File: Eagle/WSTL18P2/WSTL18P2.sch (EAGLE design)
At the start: 23 parts, among them CON1 1X6CONN-1.27-ROUND, CON2 1X6CONN-1.27-ROUND, CON3 1X6CONN-1.27-ROUND, CON4 1X6CONN-1.27-ROUND, T1 ABS07AIG

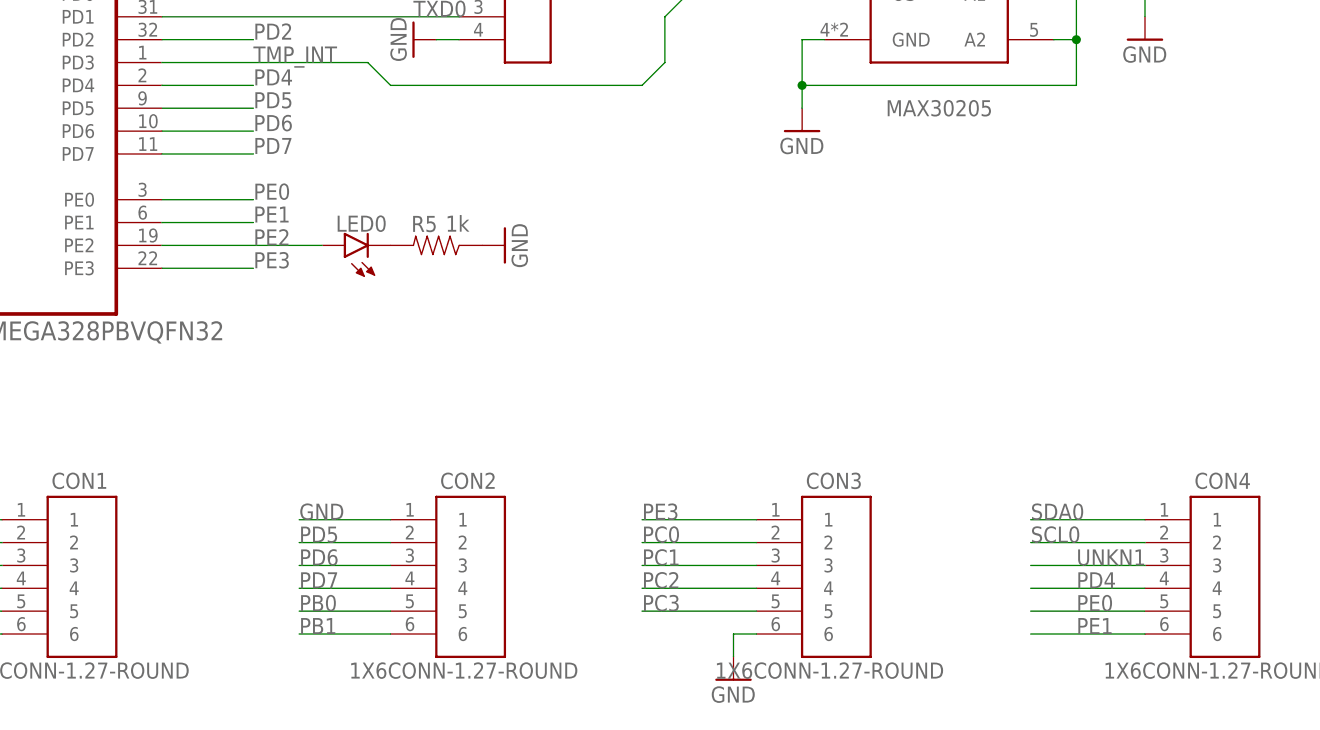
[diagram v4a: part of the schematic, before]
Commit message: Chaned LED pin, added VCC and GND next to TWI(I2C) headers, changed some traces to 8mil
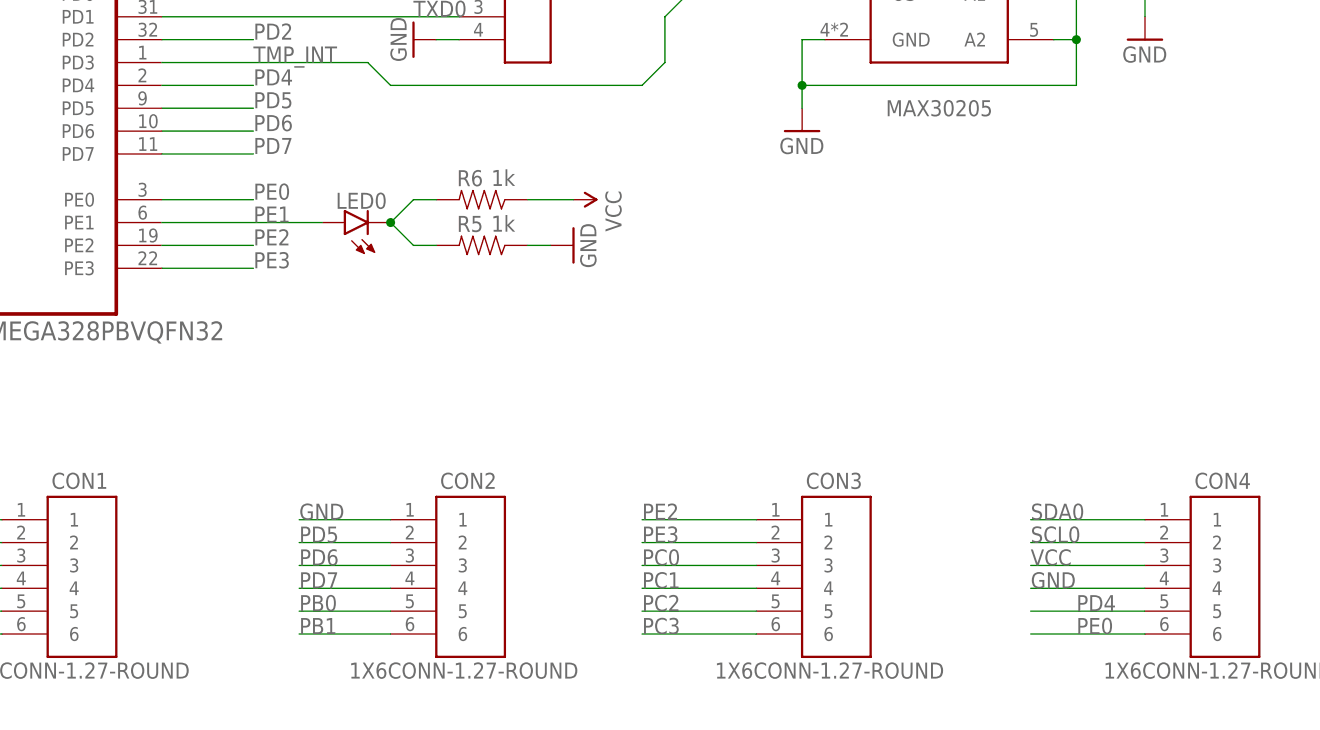
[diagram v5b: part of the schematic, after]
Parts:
- added R6: 1k, Passives:RES_0402_CERAMIC
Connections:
- removed net UNKN1: CON4.3
- net GND: now also CON4.4; no longer CON3.6
- net N$4: now also R6.1
- net PC0: now also CON3.3; no longer CON3.2
- net PC1: now also CON3.4; no longer CON3.3
- net PC2: now also CON3.5; no longer CON3.4
- net PC3: now also CON3.6; no longer CON3.5
- net PD4: now also CON4.5; no longer CON4.4
- net PE0: now also CON4.6; no longer CON4.5
- net PE1: now also LED0.A; no longer CON4.6
- net PE2: now also CON3.1; no longer LED0.A
- net PE3: now also CON3.2; no longer CON3.1
- net VCC: now also CON4.3, R6.2
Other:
- moved on the sheet: LED0, R5
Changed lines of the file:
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@@
 <part name="CON2" library="AVR_ISP_127" deviceset="1X6CONN-1.27-ROUND" device=""/>
 <part name="CON3" library="AVR_ISP_127" deviceset="1X6CONN-1.27-ROUND" device=""/>
-<part name="GND9" library="SparkFun-Aesthetics" deviceset="GND" device=""/>
 <part name="CON4" library="AVR_ISP_127" deviceset="1X6CONN-1.27-ROUND" device=""/>
 <part name="VCC" library="SparkFun-Aesthetics" deviceset="5V" device="" value="VCC"/>
@@
 <part name="GND10" library="SparkFun-Aesthetics" deviceset="GND" device=""/>
 <part name="GND12" library="SparkFun-Aesthetics" deviceset="GND" device=""/>
+<part name="VCC1" library="SparkFun-Aesthetics" deviceset="5V" device="" value="VCC"/>
+<part name="R6" library="Passives" deviceset="RES_0402_CERAMIC" device="" value="1k"/>
 </parts>
 <sheets>
@@
 </instance>
 <instance part="R1" gate="G$1" x="50.8" y="-12.7" rot="R90"/>
-<instance part="LED0" gate="G$1" x="106.68" y="22.86" smashed="yes" rot="R90">
-<attribute name="NAME" x="105.664" y="24.384" size="1.778" layer="95"/>
-</instance>
-<instance part="GND8" gate="1" x="124.46" y="22.86" rot="R90"/>
-<instance part="R5" gate="G$1" x="116.84" y="22.86" smashed="yes" rot="R180">
-<attribute name="NAME" x="114.046" y="24.3586" size="1.778" layer="95"/>
-<attribute name="VALUE" x="117.856" y="24.384" size="1.778" layer="96"/>
+<instance part="LED0" gate="G$1" x="106.68" y="25.4" smashed="yes" rot="R90">
+<attribute name="NAME" x="105.664" y="26.924" size="1.778" layer="95"/>
+</instance>
+<instance part="GND8" gate="1" x="132.08" y="22.86" rot="R90"/>
+<instance part="R5" gate="G$1" x="121.92" y="22.86" smashed="yes" rot="R180">
+<attribute name="NAME" x="119.126" y="24.3586" size="1.778" layer="95"/>
+<attribute name="VALUE" x="122.936" y="24.384" size="1.778" layer="96"/>
 </instance>
 <instance part="R4" gate="G$1" x="154.94" y="68.58" smashed="yes" rot="R90">
@@
 <instance part="CON2" gate="G$1" x="121.92" y="-10.16"/>
 <instance part="CON3" gate="G$1" x="162.56" y="-10.16"/>
-<instance part="GND9" gate="1" x="149.86" y="-25.4"/>
 <instance part="CON4" gate="G$1" x="205.74" y="-10.16"/>
 <instance part="VCC" gate="G$1" x="-76.2" y="76.2"/>
@@
 <instance part="GND10" gate="1" x="43.18" y="12.7"/>
 <instance part="GND12" gate="1" x="17.78" y="12.7"/>
+<instance part="VCC1" gate="G$1" x="132.08" y="27.94" rot="R270"/>
+<instance part="R6" gate="G$1" x="121.92" y="27.94" smashed="yes" rot="R180">
+<attribute name="NAME" x="119.126" y="29.4386" size="1.778" layer="95"/>
+<attribute name="VALUE" x="122.936" y="29.464" size="1.778" layer="96"/>
+</instance>
 </instances>
 <busses>
@@
 <wire x1="48.26" y1="76.2" x2="48.26" y2="71.12" width="0.1524" layer="91"/>
 <junction x="48.26" y="71.12"/>
+</segment>
+<segment>
+<pinref part="R6" gate="G$1" pin="2"/>
+<pinref part="VCC1" gate="G$1" pin="5V"/>
+<wire x1="127" y1="27.94" x2="132.08" y2="27.94" width="0.1524" layer="91"/>
+</segment>
+<segment>
+<label x="182.88" y="-12.7" size="1.778" layer="95"/>
+<wire x1="182.88" y1="-12.7" x2="195.58" y2="-12.7" width="0.1524" layer="91"/>
+<pinref part="CON4" gate="G$1" pin="3"/>
 </segment>
 </net>
@@
 <pinref part="GND8" gate="1" pin="GND"/>
 <pinref part="R5" gate="G$1" pin="2"/>
+<wire x1="127" y1="22.86" x2="129.54" y2="22.86" width="0.1524" layer="91"/>
 </segment>
 <segment>
@@
 </segment>
 <segment>
-<pinref part="GND9" gate="1" pin="GND"/>
-<wire x1="149.86" y1="-20.32" x2="149.86" y2="-22.86" width="0.1524" layer="91"/>
-<pinref part="CON3" gate="G$1" pin="6"/>
-<wire x1="149.86" y1="-20.32" x2="152.4" y2="-20.32" width="0.1524" layer="91"/>
-</segment>
-<segment>
 <pinref part="GND11" gate="1" pin="GND"/>
 <pinref part="UART" gate="G$1" pin="4"/>
@@
 <pinref part="C7" gate="G$1" pin="2"/>
 <wire x1="43.18" y1="15.24" x2="43.18" y2="17.78" width="0.1524" layer="91"/>
+</segment>
+<segment>
+<pinref part="CON4" gate="G$1" pin="4"/>
+<wire x1="195.58" y1="-15.24" x2="182.88" y2="-15.24" width="0.1524" layer="91"/>
+<label x="182.88" y="-15.24" size="1.778" layer="95"/>
 </segment>
 </net>
@@
 <pinref part="LED0" gate="G$1" pin="C"/>
 <pinref part="R5" gate="G$1" pin="1"/>
+<wire x1="111.76" y1="25.4" x2="114.3" y2="22.86" width="0.1524" layer="91"/>
+<wire x1="114.3" y1="22.86" x2="116.84" y2="22.86" width="0.1524" layer="91"/>
+<wire x1="111.76" y1="25.4" x2="114.3" y2="27.94" width="0.1524" layer="91"/>
+<junction x="111.76" y="25.4"/>
+<pinref part="R6" gate="G$1" pin="1"/>
+<wire x1="114.3" y1="27.94" x2="116.84" y2="27.94" width="0.1524" layer="91"/>
 </segment>
 </net>
@@
 </segment>
 <segment>
-<label x="187.96" y="-15.24" size="1.778" layer="95"/>
-<pinref part="CON4" gate="G$1" pin="4"/>
-<wire x1="182.88" y1="-15.24" x2="195.58" y2="-15.24" width="0.1524" layer="91"/>
+<label x="187.96" y="-17.78" size="1.778" layer="95"/>
+<wire x1="182.88" y1="-17.78" x2="195.58" y2="-17.78" width="0.1524" layer="91"/>
+<pinref part="CON4" gate="G$1" pin="5"/>
 </segment>
 </net>
@@
 </segment>
 <segment>
-<label x="187.96" y="-17.78" size="1.778" layer="95"/>
-<wire x1="182.88" y1="-17.78" x2="195.58" y2="-17.78" width="0.1524" layer="91"/>
-<pinref part="CON4" gate="G$1" pin="5"/>
+<label x="187.96" y="-20.32" size="1.778" layer="95"/>
+<wire x1="182.88" y1="-20.32" x2="195.58" y2="-20.32" width="0.1524" layer="91"/>
+<pinref part="CON4" gate="G$1" pin="6"/>
 </segment>
 </net>
@@
 <segment>
 <pinref part="MCU" gate="A" pin="PE1"/>
-<wire x1="86.36" y1="25.4" x2="96.52" y2="25.4" width="0.1524" layer="91"/>
+<wire x1="86.36" y1="25.4" x2="104.14" y2="25.4" width="0.1524" layer="91"/>
 <label x="96.52" y="25.4" size="1.778" layer="95"/>
-</segment>
-<segment>
-<wire x1="195.58" y1="-20.32" x2="182.88" y2="-20.32" width="0.1524" layer="91"/>
-<label x="187.96" y="-20.32" size="1.778" layer="95"/>
-<pinref part="CON4" gate="G$1" pin="6"/>
+<pinref part="LED0" gate="G$1" pin="A"/>
 </segment>
 </net>
@@
 </segment>
 <segment>
-<wire x1="152.4" y1="-7.62" x2="139.7" y2="-7.62" width="0.1524" layer="91"/>
-<label x="139.7" y="-7.62" size="1.778" layer="95"/>
-<pinref part="CON3" gate="G$1" pin="1"/>
+<label x="139.7" y="-10.16" size="1.778" layer="95"/>
+<wire x1="152.4" y1="-10.16" x2="139.7" y2="-10.16" width="0.1524" layer="91"/>
+<pinref part="CON3" gate="G$1" pin="2"/>
 </segment>
 </net>
@@
 </segment>
 <segment>
-<pinref part="CON3" gate="G$1" pin="3"/>
-<wire x1="152.4" y1="-12.7" x2="139.7" y2="-12.7" width="0.1524" layer="91"/>
-<label x="139.7" y="-12.7" size="1.778" layer="95"/>
+<label x="139.7" y="-15.24" size="1.778" layer="95"/>
+<wire x1="152.4" y1="-15.24" x2="139.7" y2="-15.24" width="0.1524" layer="91"/>
+<pinref part="CON3" gate="G$1" pin="4"/>
 </segment>
 </net>
@@
 </segment>
 <segment>
-<wire x1="152.4" y1="-10.16" x2="139.7" y2="-10.16" width="0.1524" layer="91"/>
-<label x="139.7" y="-10.16" size="1.778" layer="95"/>
-<pinref part="CON3" gate="G$1" pin="2"/>
+<label x="139.7" y="-12.7" size="1.778" layer="95"/>
+<wire x1="152.4" y1="-12.7" x2="139.7" y2="-12.7" width="0.1524" layer="91"/>
+<pinref part="CON3" gate="G$1" pin="3"/>
 </segment>
 </net>
@@
 </segment>
 <segment>
-<wire x1="152.4" y1="-17.78" x2="139.7" y2="-17.78" width="0.1524" layer="91"/>
-<label x="139.7" y="-17.78" size="1.778" layer="95"/>
-<pinref part="CON3" gate="G$1" pin="5"/>
-</segment>
-</net>
-<net name="PE2" class="0">
-<segment>
-<pinref part="MCU" gate="A" pin="PE2"/>
-<wire x1="86.36" y1="22.86" x2="104.14" y2="22.86" width="0.1524" layer="91"/>
-<label x="96.52" y="22.86" size="1.778" layer="95"/>
-<pinref part="LED0" gate="G$1" pin="A"/>
+<label x="139.7" y="-20.32" size="1.778" layer="95"/>
+<wire x1="152.4" y1="-20.32" x2="139.7" y2="-20.32" width="0.1524" layer="91"/>
+<pinref part="CON3" gate="G$1" pin="6"/>
 </segment>
 </net>
@@
 </segment>
 <segment>
-<wire x1="152.4" y1="-15.24" x2="139.7" y2="-15.24" width="0.1524" layer="91"/>
-<label x="139.7" y="-15.24" size="1.778" layer="95"/>
-<pinref part="CON3" gate="G$1" pin="4"/>
-</segment>
-</net>
-<net name="UNKN1" class="0">
-<segment>
-<label x="187.96" y="-12.7" size="1.778" layer="95"/>
-<wire x1="182.88" y1="-12.7" x2="195.58" y2="-12.7" width="0.1524" layer="91"/>
-<pinref part="CON4" gate="G$1" pin="3"/>
+<label x="139.7" y="-17.78" size="1.778" layer="95"/>
+<wire x1="152.4" y1="-17.78" x2="139.7" y2="-17.78" width="0.1524" layer="91"/>
+<pinref part="CON3" gate="G$1" pin="5"/>
 </segment>
 </net>
@@
 </segment>
 </net>
+<net name="PE2" class="0">
+<segment>
+<pinref part="MCU" gate="A" pin="PE2"/>
+<wire x1="86.36" y1="22.86" x2="96.52" y2="22.86" width="0.1524" layer="91"/>
+<label x="96.52" y="22.86" size="1.778" layer="95"/>
+</segment>
+<segment>
+<pinref part="CON3" gate="G$1" pin="1"/>
+<wire x1="152.4" y1="-7.62" x2="139.7" y2="-7.62" width="0.1524" layer="91"/>
+<label x="139.7" y="-7.62" size="1.778" layer="95"/>
+</segment>
+</net>

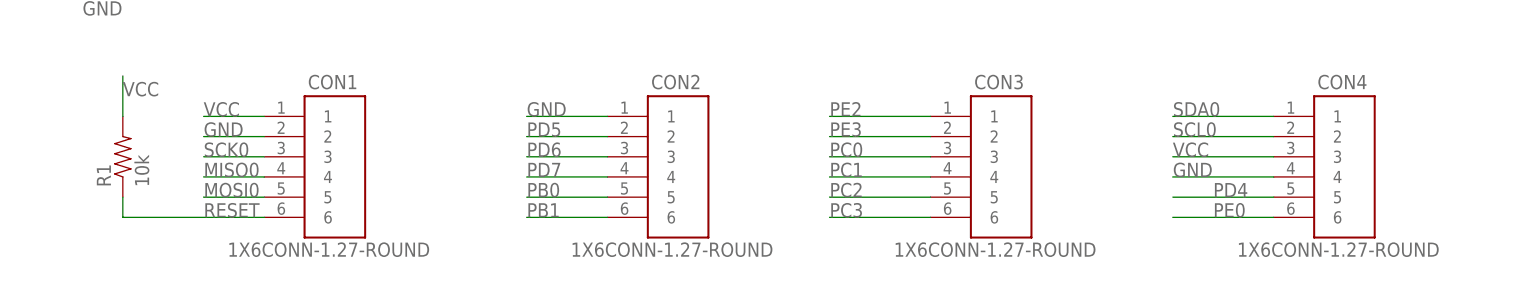
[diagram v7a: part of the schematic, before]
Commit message: Center-alligned all 4 6-wire headers
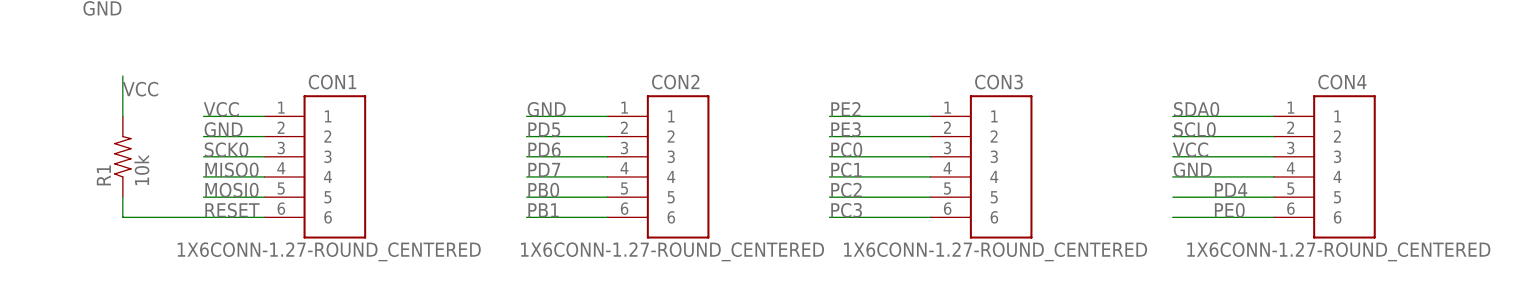
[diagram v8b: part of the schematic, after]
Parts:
- CON1, CON2, CON3, CON4: value 1X6CONN-1.27-ROUND -> 1X6CONN-1.27-ROUND_CENTERED; device AVR_ISP_127:1X6CONN-1.27-ROUND -> AVR_ISP_127:1X6CONN-1.27-ROUND_CENTERED
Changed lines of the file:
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@@
 <part name="R5" library="Passives" deviceset="RES_0402_CERAMIC" device="" value="1k"/>
 <part name="R4" library="Passives" deviceset="RES_0402_CERAMIC" device="" value="4.7k"/>
-<part name="CON1" library="AVR_ISP_127" deviceset="1X6CONN-1.27-ROUND" device=""/>
-<part name="CON2" library="AVR_ISP_127" deviceset="1X6CONN-1.27-ROUND" device=""/>
-<part name="CON3" library="AVR_ISP_127" deviceset="1X6CONN-1.27-ROUND" device=""/>
-<part name="CON4" library="AVR_ISP_127" deviceset="1X6CONN-1.27-ROUND" device=""/>
+<part name="CON1" library="AVR_ISP_127" deviceset="1X6CONN-1.27-ROUND_CENTERED" device=""/>
+<part name="CON2" library="AVR_ISP_127" deviceset="1X6CONN-1.27-ROUND_CENTERED" device=""/>
+<part name="CON3" library="AVR_ISP_127" deviceset="1X6CONN-1.27-ROUND_CENTERED" device=""/>
+<part name="CON4" library="AVR_ISP_127" deviceset="1X6CONN-1.27-ROUND_CENTERED" device=""/>
 <part name="VCC" library="SparkFun-Aesthetics" deviceset="5V" device="" value="VCC"/>
 <part name="GND11" library="SparkFun-Aesthetics" deviceset="GND" device=""/>
